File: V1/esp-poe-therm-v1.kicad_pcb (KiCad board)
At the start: 2 copper layers, 66 x 45 mm, 80 parts, among them J1 USB_C_Receptacle_USB2.0, J2 RJ45 JACK, J3 PT1000 RTD, Q1 UMH3N, Q2 WPM2015-3/TR, Q3 LMUN2211LT1G, SW1 RESET, U1 TPS2376DDAR-H, U2 TX4138, U3 SY8089A1AAC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

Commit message: Lots of stuff
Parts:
- R25: value 4,02k/100mW -> 4,02k/62,5mW; footprint Tales:R_0603_1608Metric -> Tales:R_0402_1005Metric
- moved R22 19.7 mm to (112.5, 94.5)
- moved C22 16.0 mm to (114.2, 93.5), turned to 90 degrees
- moved R21 15.6 mm to (110.8, 81.5), turned to 180 degrees
- moved R25 9.57 mm to (78.2, 101.0)
- moved R23 7.15 mm to (106.5, 94.0), turned to 0 degrees
- moved R24 4.27 mm to (108.5, 94.0), turned to 0 degrees
- moved C24 2.50 mm to (110.5, 89.0)
- moved C25 2.26 mm to (104.2, 92.2)
- moved L3 2.26 mm to (104.2, 88.9)
- moved Q2 2.25 mm to (107.2, 88.5)
- moved Q3 2.25 mm to (107.2, 92.0)
- moved D1 2.24 mm to (116.5, 110.0)
- moved R11 2.00 mm to (127.9, 82.0)
- moved C1 2.00 mm to (119.2, 110.0)
- moved C15 2.00 mm to (102.0, 74.8)
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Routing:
- net +3.3V: track 129.3 -> 112.0 mm, vias 7 -> 6
- net /LED_G_K: track 19.2 -> 1.95 mm
- net Net-(J2-RLED-): track 26.5 -> 42.7 mm
- net Net-(J2-LLED-): track 7.07 -> 18.4 mm
- net /LED_Y_A: track 37.1 -> 44.1 mm
- net Net-(Q2-G): track 5.63 -> 11.3 mm
- net Net-(U8-BIAS): track 3.50 -> 8.86 mm
- net Net-(J2-SHIELD): track 20.3 -> 24.9 mm, vias 1 -> 0
- net PoE+: track 42.3 -> 38.8 mm
- net Net-(C10-Pad1): track 71.9 -> 69.4 mm
- net SPI_CS: track 18.8 -> 16.8 mm
- net Net-(U8-ISENSOR): track 7.62 -> 5.66 mm
- net GND: track 84.7 -> 86.6 mm
- net Net-(Q1B-C2): track 8.18 -> 6.37 mm
- net SPI_MISO: track 23.6 -> 22.3 mm
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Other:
- board size 66 x 45 mm -> 64 x 45 mm

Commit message: Finishing touches
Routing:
- net GND: track 86.6 -> 100.5 mm
- net +3.3V: track 112.0 -> 119.9 mm, vias 6 -> 7
- net PoE+: track 38.8 -> 40.3 mm
- net +3.3VLAN: track 43.8 -> 44.8 mm, vias 6 -> 5

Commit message: Replace ESP32 for externa antena version
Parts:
- U5: value ESP32-WROOM-32E-N4 -> ESP32-WROOM-32UE-N4; footprint Tales:ESP32-WROOM-32 -> Tales:ESP32-WROOM-32U

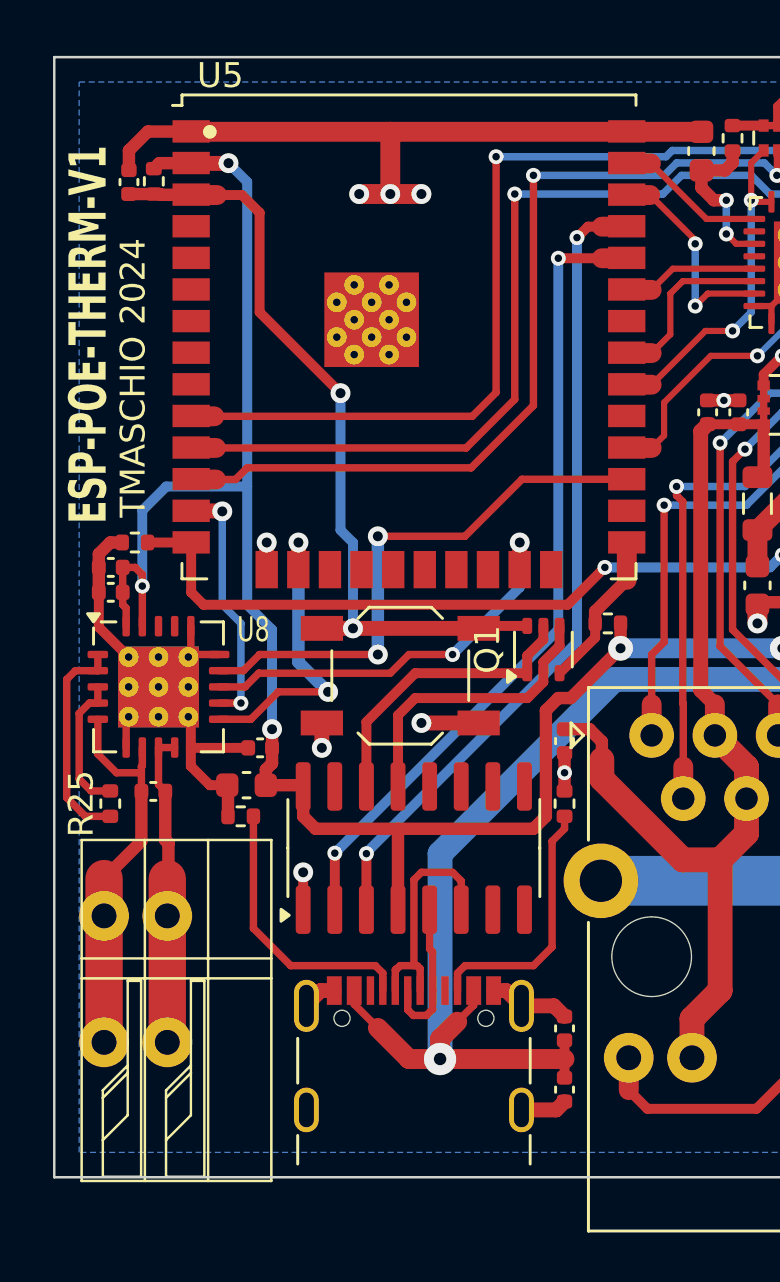
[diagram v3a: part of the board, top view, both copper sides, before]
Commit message: Replace sensor type
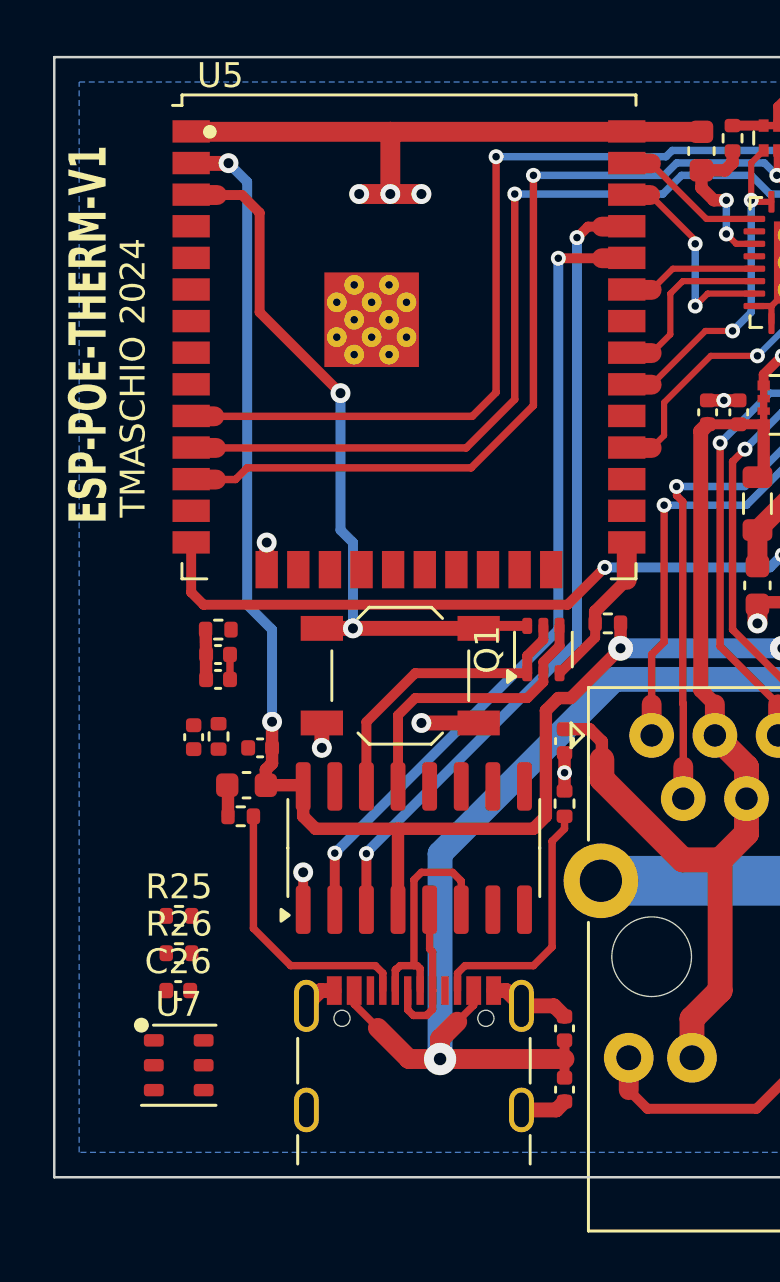
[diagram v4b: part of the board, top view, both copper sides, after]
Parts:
- removed C28: 10nF/50V, Tales:C_0402_1005Metric
- removed J3: PT1000 RTD, Tales:TerminalBlock_Dibo_DB141R-2.54-2P_1x02_P2.54mm_Horizontal
- removed U8: MAX31865xTP, Tales:TQFN-20-1EP_5x5mm_P0.65mm_EP3.25x3.25mm_ThermalVias
- added C26: 100nF/50V, Tales:C_0402_1005Metric, F.Cu at (81.0, 108.5)
- added R26: 2k2/62,5mW, Tales:R_0402_1005Metric, F.Cu at (81.0, 107.0)
- added U7: AHT20, Tales:DFN-6-3x3mm_P1mm, F.Cu at (81.0, 111.5)
- R25: value 4,02k/62,5mW -> 2k2/62,5mW
- moved R16 22.5 mm to (82.6, 98.3)
- moved C14 22.5 mm to (81.6, 98.3)
- moved C27 5.55 mm to (82.6, 95.0)
- moved C29 5.55 mm to (82.6, 96.0)
- moved R25 5.29 mm to (81.0, 105.5), turned to 0 degrees
- moved R18 4.84 mm to (82.6, 94.0)
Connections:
- R25 pad 1: Net-(U8-BIAS) -> +3.3V
- R25 pad 2: Net-(U8-ISENSOR) -> /I2C_SCL
- U5 pad 13: SPI_CLK -> unconnected-(U5-IO14-Pad13)
- U5 pad 16: SPI_MOSI -> unconnected-(U5-IO13-Pad16)
- U5 pad 23: SPI_CS -> unconnected-(U5-IO15-Pad23)
- U5 pad 27: SPI_MISO -> unconnected-(U5-IO16-Pad27)
- U5 pad 8: unconnected-(U5-IO32-Pad8) -> /I2C_SCL
- U5 pad 9: unconnected-(U5-IO33-Pad9) -> /I2C_SDA
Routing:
- net SPI_MISO: track 22.3 -> 0.00 mm, vias 2 -> 0
- net SPI_CS: track 16.8 -> 0.00 mm, vias 2 -> 0
- net GND: track 100.5 -> 83.9 mm
- net Net-(J3-Pin_1): track 15.9 -> 0.00 mm
- net +3.3V: track 119.9 -> 106.3 mm, vias 7 -> 6
- net Net-(J3-Pin_2): track 12.7 -> 0.00 mm
- net SPI_MOSI: track 12.6 -> 0.00 mm, vias 2 -> 0
- net SPI_CLK: track 10.1 -> 0.00 mm, vias 2 -> 0
- net Net-(U8-BIAS): track 8.86 -> 0.00 mm
- net Net-(U8-ISENSOR): track 5.66 -> 0.00 mm
- net Net-(Q1A-C1): track 32.1 -> 29.6 mm
- net PHY_PWR: track 29.5 -> 27.8 mm

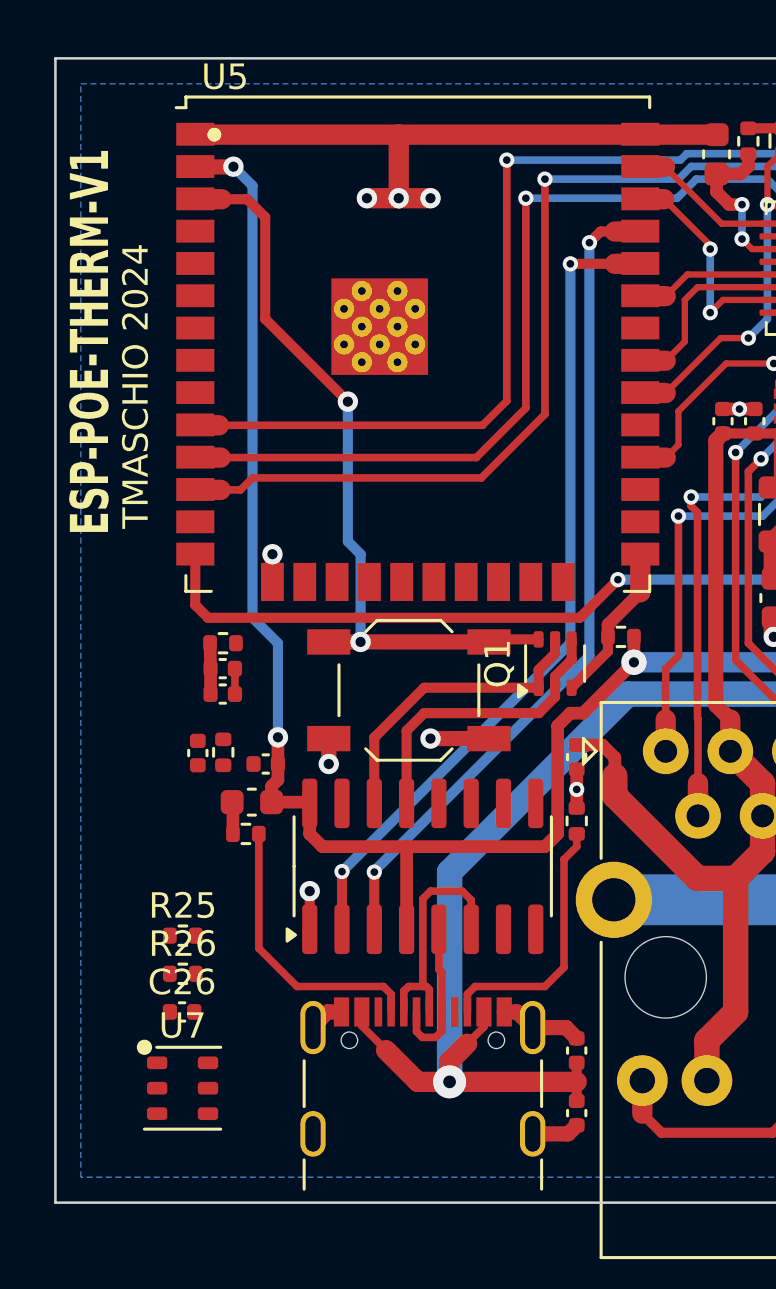
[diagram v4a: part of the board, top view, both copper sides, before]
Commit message: Replacing external for onboard sensor
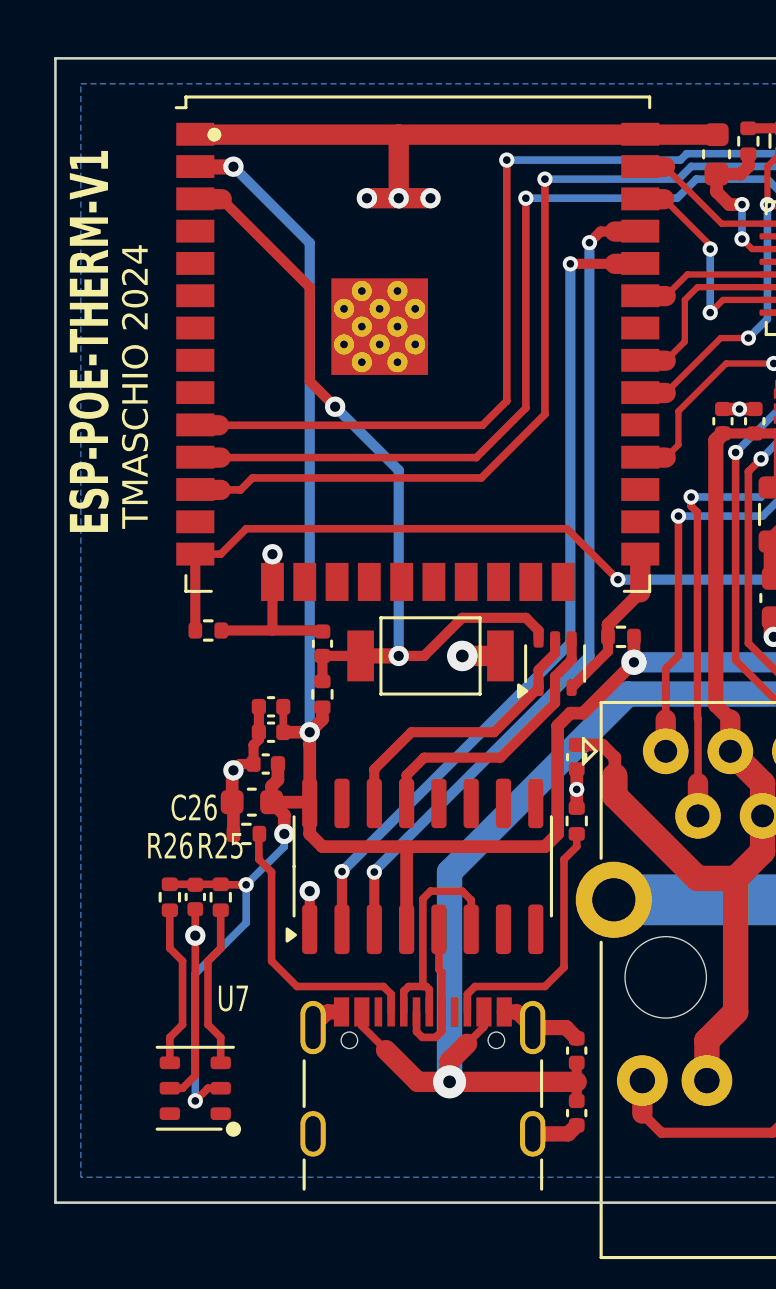
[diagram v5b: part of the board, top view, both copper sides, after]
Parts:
- SW1: footprint Tales:SW_SPST_TL3342 -> Tales:SW_SPST_Xunpu_TS1088AR02016
- moved C14 6.52 mm to (86.5, 94.0)
- moved C26 4.55 mm to (81.5, 104.0), turned to -90 degrees
- moved R16 4.52 mm to (86.5, 96.0), turned to 90 degrees
- moved R26 3.05 mm to (80.5, 104.0), turned to -90 degrees
- moved C27 2.42 mm to (84.5, 96.5)
- moved C29 2.42 mm to (84.5, 97.5)
- moved R25 2.12 mm to (82.5, 104.0), turned to -90 degrees
- moved SW1 1.60 mm to (90.8, 94.5)
- moved R18 0.77 mm to (82.0, 93.5), turned to 180 degrees
- moved U7 0.50 mm to (81.5, 111.5), turned to 180 degrees
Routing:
- net +3.3V: track 106.3 -> 128.2 mm, vias 6 -> 9
- net GND: track 83.9 -> 98.3 mm, vias 31 -> 32
- net /I2C_SDA: track 0.00 -> 6.41 mm
- net /I2C_SCL: track 0.00 -> 6.41 mm
- net Net-(Q1A-C1): track 29.6 -> 32.6 mm
- net PHY_PWR: track 27.8 -> 29.2 mm
- net Net-(Q1A-E1): track 12.0 -> 11.3 mm
- net Net-(Q1A-B1): track 11.5 -> 10.9 mm

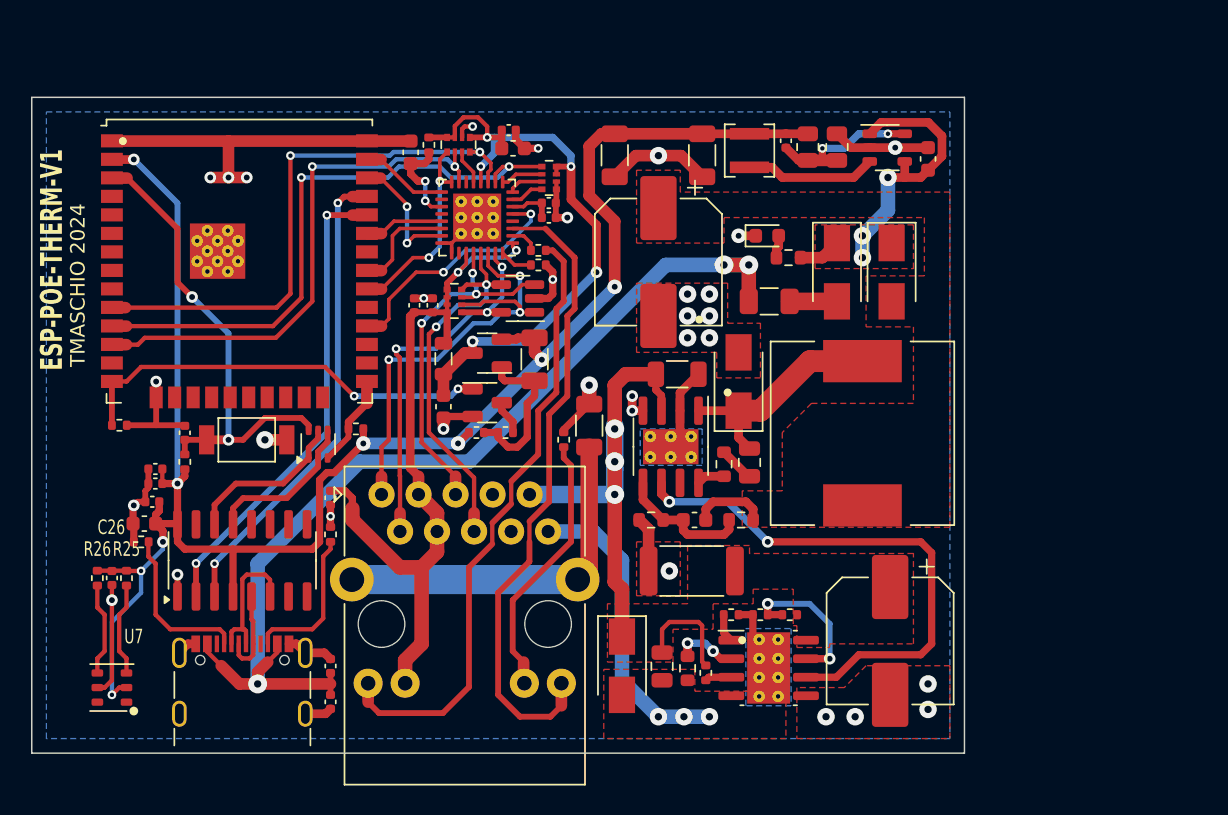
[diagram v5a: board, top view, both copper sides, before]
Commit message: Updating sensor type
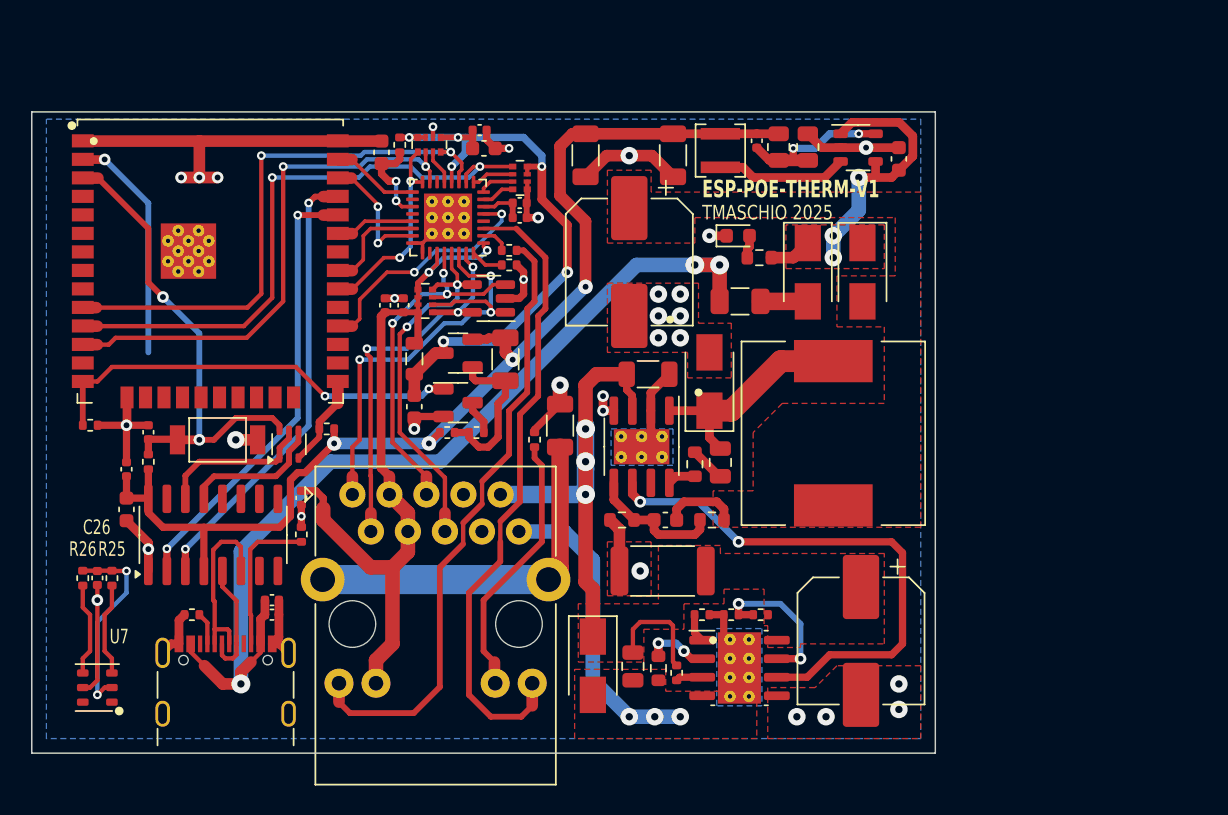
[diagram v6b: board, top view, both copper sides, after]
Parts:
- removed C27, C29: 100nF/50V, Tales:C_0402_1005Metric
- moved C10 7.21 mm to (92.5, 106.5), turned to 0 degrees
- moved R14 6.09 mm to (87.0, 106.5)
- moved C11 6.05 mm to (92.5, 105.5), turned to 0 degrees
- moved C13 2.85 mm to (82.5, 96.5), turned to 90 degrees
- moved U4 2.66 mm to (88.4, 101.0)
- moved C14 2.50 mm to (84.0, 94.0)
- moved R16 2.50 mm to (84.0, 96.0)
- moved C1 2.00 mm to (117.2, 110.0)
- moved C15 2.00 mm to (100.0, 74.8)
- moved C16 2.00 mm to (101.5, 85.3)
- moved C17 2.00 mm to (106.7, 73.2)
- moved C18 2.00 mm to (100.2, 85.3)
- moved C19 2.00 mm to (107.0, 74.5)
- moved C2 2.00 mm to (132.9, 108.3)
- moved C20 2.00 mm to (109.5, 79.2)
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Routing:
- net +3.3V: track 128.2 -> 109.1 mm, vias 9 -> 7
- net Net-(J1-CC1): track 11.2 -> 2.23 mm
- net Net-(C10-Pad1): track 69.4 -> 65.6 mm
- net /USB_D-: track 9.60 -> 12.3 mm
- net /USB_D+: track 6.02 -> 8.12 mm
- net Net-(U4-TXD): track 32.6 -> 30.9 mm
- net Net-(U4-RXD): track 32.7 -> 31.0 mm
- net GND: track 98.3 -> 96.9 mm, vias 32 -> 31
- net Net-(Q1A-B1): track 10.9 -> 9.88 mm
- net +3.3VLAN: track 44.8 -> 43.9 mm, vias 5 -> 6
- net Net-(Q1A-E1): track 11.3 -> 10.7 mm
- net Net-(Q1A-C1): track 32.6 -> 33.1 mm
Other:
- board size 64 x 45 mm -> 62 x 44 mm
- board text added: "TMASCHIO 2025"
- board text removed: "TMASCHIO 2024"

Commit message: Layout updated
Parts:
- moved C1 2.00 mm to (115.2, 110.0)
- moved C10 2.00 mm to (90.5, 106.5)
- moved C11 2.00 mm to (90.5, 105.5)
- moved C12 2.00 mm to (80.5, 99.3)
- moved C13 2.00 mm to (80.5, 96.5)
- moved C14 2.00 mm to (82.0, 94.0)
- moved C15 2.00 mm to (98.0, 74.8)
- moved C16 2.00 mm to (99.5, 85.3)
- moved C18 2.00 mm to (98.2, 85.3)
- moved C19 2.00 mm to (105.0, 74.5)
- moved C2 2.00 mm to (130.9, 108.3)
- moved C20 2.00 mm to (107.5, 79.2)
- moved C21 2.00 mm to (107.5, 78.2)
- moved C22 2.00 mm to (110.2, 93.5)
- moved C23 2.00 mm to (92.5, 98.5)
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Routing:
- net GND: track 96.9 -> 96.2 mm
- net +3.3VLAN: track 43.9 -> 44.4 mm
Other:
- board size 62 x 44 mm -> 60 x 44 mm

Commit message: dev
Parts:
- added J3: Sensor Temperatura, Connector_JST:JST_PH_B4B-PH-K_1x04_P2.00mm_Vertical, F.Cu at (78.5, 113.5)
- added J4: Sensor Temperatura, Connector_JST:JST_PH_S4B-PH-K_1x04_P2.00mm_Horizontal, F.Cu at (152.5, 98.5)
- moved C26 71.4 mm to (149.5, 111.5), turned to 0 degrees
- moved U7 71.0 mm to (149.5, 109.0), turned to 0 degrees
- moved R25 7.06 mm to (78.5, 97.0), turned to 180 degrees
- moved R26 5.58 mm to (78.5, 98.5), turned to 180 degrees
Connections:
- C26 pad 1: +3.3V -> Net-(J4-Pin_4)
- C26 pad 2: GND -> Net-(J4-Pin_1)
- U7 pad 2: +3.3V -> Net-(J4-Pin_4)
- U7 pad 3: /I2C_SCL -> Net-(J4-Pin_3)
- U7 pad 4: /I2C_SDA -> Net-(J4-Pin_2)
- U7 pad 5: GND -> Net-(J4-Pin_1)
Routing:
- net /I2C_SCL: track 6.41 -> 38.5 mm, vias 0 -> 2
- net /I2C_SDA: track 6.41 -> 31.9 mm, vias 0 -> 2
- net Net-(J4-Pin_1): track 0.00 -> 15.7 mm
- net Net-(J4-Pin_4): track 0.00 -> 15.6 mm
- net Net-(J4-Pin_2): track 0.00 -> 12.4 mm
- net Net-(J4-Pin_3): track 0.00 -> 12.4 mm
- net GND: track 96.2 -> 88.5 mm, vias 31 -> 30
- net +3.3V: track 109.1 -> 114.2 mm, vias 7 -> 5
- added copper zone on B.Cu, net Net-(J4-Pin_4)
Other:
- board size 60 x 44 mm -> 80 x 44 mm
- board text added: "GND"
- board text added: "SCL"
- board text added: "SDA"
- board text added: "VDD"
